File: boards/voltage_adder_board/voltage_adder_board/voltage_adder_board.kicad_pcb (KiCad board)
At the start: 2 copper layers, 95.8 x 94 mm, 30 parts, among them J1 Conn_01x02_Female, J2 Conn_01x04, J3 Conn_01x02_Female, J4 Conn_01x02_Female, J5 Conn_01x03_Female, J6 Conn_01x03_Female, U1 UA741CP, U2 UA741CP, U3 UA741CP

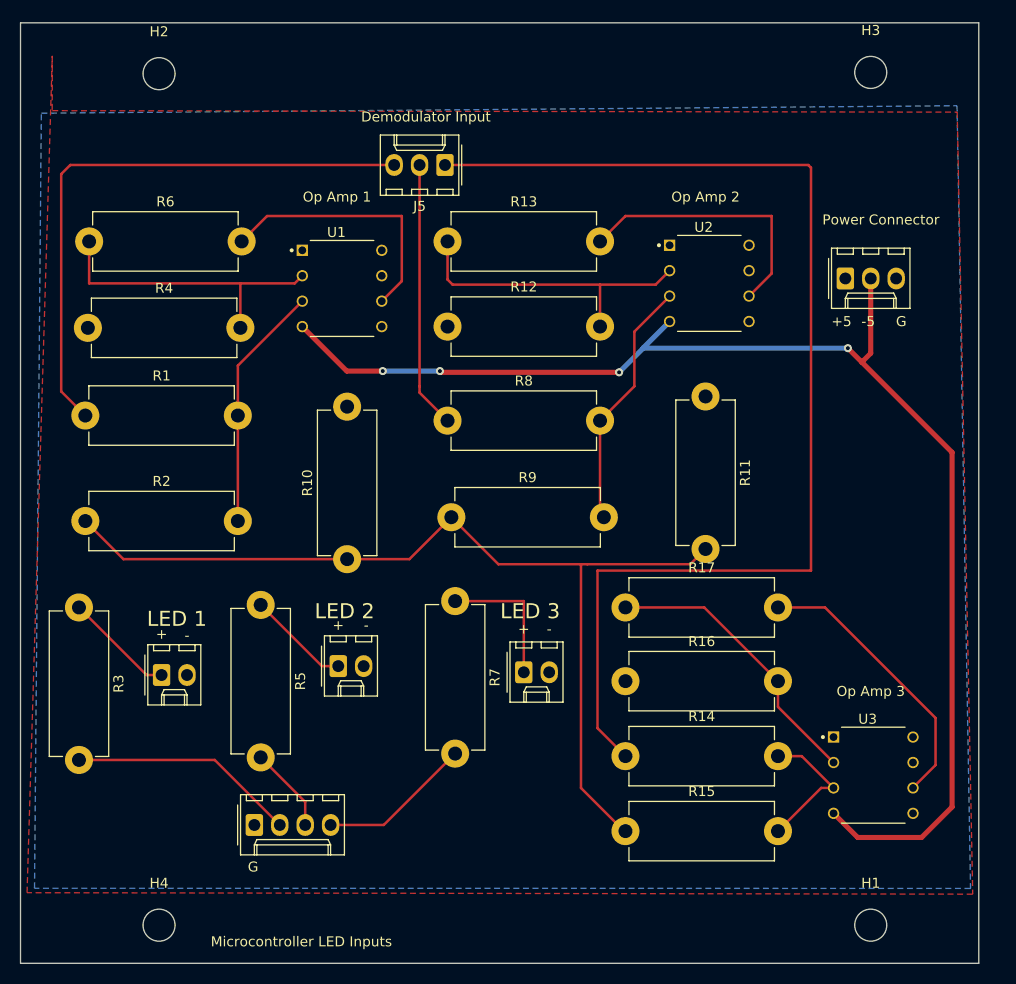
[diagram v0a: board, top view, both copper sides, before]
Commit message: finished voltage adder board
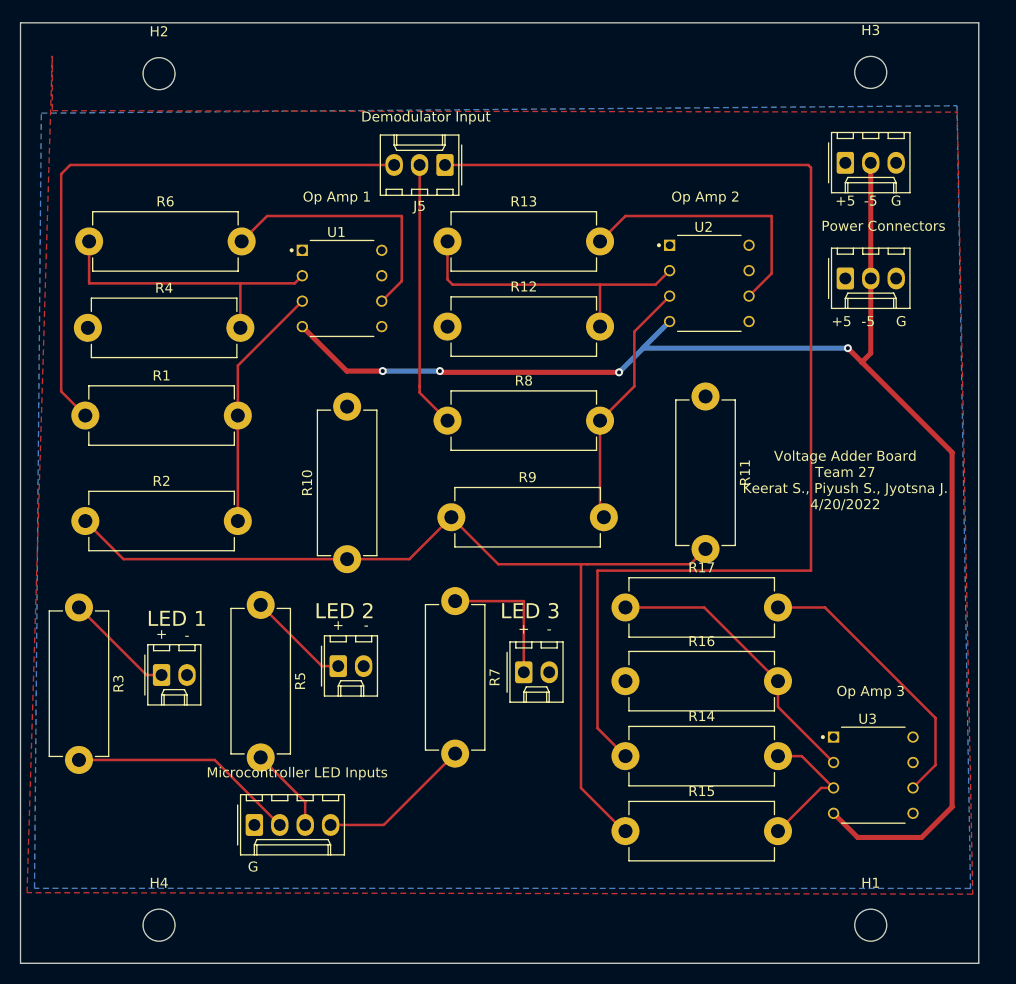
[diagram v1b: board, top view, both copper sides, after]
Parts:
- added J7: Conn_01x03_Female, Connector_Molex:Molex_KK-254_AE-6410-03A_1x03_P2.54mm_Vertical, F.Cu at (144.8, 50.8)
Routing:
- net -5V: track 134.2 -> 145.8 mm
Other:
- board text added: "Power Connectors"
- board text added: "Voltage Adder Board Team 27 Keerat S., Piyush S., Jyotsna J. 4/20/2022"
- board text removed: "Power Connector"
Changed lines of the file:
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@@
   (net 25 "unconnected-(U3-Pad1)")
   (net 26 "unconnected-(U3-Pad5)")
-  (net 27 "Net-(R5-Pad2)")
-  (net 28 "Net-(R7-Pad2)")
+  (net 27 "Net-(J2-Pad3)")
+  (net 28 "Net-(J2-Pad4)")
   (footprint "Resistor_THT:R_Axial_DIN0614_L14.3mm_D5.7mm_P15.24mm_Horizontal" (layer "F.Cu")
     (at 69.088 67.31)
@@
       (net 4 "Net-(J3-Pad1)") (pintype "passive"))
     (pad "2" thru_hole oval (at 15.24 0 270) (size 2.8 2.8) (drill 1.4) (layers *.Cu *.Mask)
-      (net 27 "Net-(R5-Pad2)") (pintype "passive"))
+      (net 27 "Net-(J2-Pad3)") (pintype "passive"))
     (model "${KICAD6_3DMODEL_DIR}/Resistor_THT.3dshapes/R_Axial_DIN0614_L14.3mm_D5.7mm_P15.24mm_Horizontal.wrl"
       (offset (xyz 0 0 0))
@@
     (fp_circle (center 0 0) (end 3.45 0) (layer "F.CrtYd") (width 0.05) (fill none))
     (pad "" np_thru_hole circle (at 0 0) (size 3.2 3.2) (drill 3.2) (layers *.Cu *.Mask))
+  )
+  (footprint "Connector_Molex:Molex_KK-254_AE-6410-03A_1x03_P2.54mm_Vertical" (layer "F.Cu")
+    (at 144.78 50.82)
+    (descr "Molex KK-254 Interconnect System, old/engineering part number: AE-6410-03A example for new part number: 22-27-2031, 3 Pins (http://www.molex.com/pdm_docs/sd/022272021_sd.pdf), generated with kicad-footprint-generator")
+    (tags "connector Molex KK-254 vertical")
+    (property "Sheetfile" "voltage_adder_board.kicad_sch")
+    (property "Sheetname" "")
+    (attr through_hole)
+    (fp_text reference "J7" (at 2.54 -4.12) (layer "F.SilkS") hide
+      (effects (font (size 1 1) (thickness 0.15)))
+    )
+    (fp_text value "Conn_01x03_Female" (at 2.794 4.715) (layer "F.Fab")
+      (effects (font (size 1 1) (thickness 0.15)))
+    )
+    (fp_text user "G" (at 5.08 3.81 unlocked) (layer "F.SilkS")
+      (effects (font (size 1 1) (thickness 0.15)))
+    )
+    (fp_text user "-5" (at 2.54 3.81 unlocked) (layer "F.SilkS")
+      (effects (font (size 1 1) (thickness 0.15)))
+    )
+    (fp_text user "+5" (at 0 3.81 unlocked) (layer "F.SilkS")
+      (effects (font (size 1 1) (thickness 0.15)))
+    )
+    (fp_text user "${REFERENCE}" (at 2.54 -2.22) (layer "F.Fab")
+      (effects (font (size 1 1) (thickness 0.15)))
+    )
+    (fp_line (start 0.8 -2.43) (end 0.8 -3.03) (layer "F.SilkS") (width 0.12))
+    (fp_line (start -1.38 2.99) (end 6.46 2.99) (layer "F.SilkS") (width 0.12))
+    (fp_line (start 4.83 1.46) (end 5.08 1.99) (layer "F.SilkS") (width 0.12))
+    (fp_line (start 0.25 2.99) (end 0.25 1.99) (layer "F.SilkS") (width 0.12))
+    (fp_line (start 4.28 -2.43) (end 5.88 -2.43) (layer "F.SilkS") (width 0.12))
+    (fp_line (start 0.25 1.46) (end 4.83 1.46) (layer "F.SilkS") (width 0.12))
+    (fp_line (start 1.74 -2.43) (end 3.34 -2.43) (layer "F.SilkS") (width 0.12))
+    (fp_line (start -0.8 -3.03) (end -0.8 -2.43) (layer "F.SilkS") (width 0.12))
+    (fp_line (start 0 2.99) (end 0 1.99) (layer "F.SilkS") (width 0.12))
+    (fp_line (start 0 1.99) (end 0.25 1.46) (layer "F.SilkS") (width 0.12))
+    (fp_line (start 4.28 -3.03) (end 4.28 -2.43) (layer "F.SilkS") (width 0.12))
+    (fp_line (start 4.83 2.99) (end 4.83 1.99) (layer "F.SilkS") (width 0.12))
+    (fp_line (start 0 1.99) (end 5.08 1.99) (layer "F.SilkS") (width 0.12))
+    (fp_line (start 5.08 1.99) (end 5.08 2.99) (layer "F.SilkS") (width 0.12))
+    (fp_line (start 3.34 -2.43) (end 3.34 -3.03) (layer "F.SilkS") (width 0.12))
+    (fp_line (start 6.46 2.99) (end 6.46 -3.03) (layer "F.SilkS") (width 0.12))
+    (fp_line (start 5.88 -2.43) (end 5.88 -3.03) (layer "F.SilkS") (width 0.12))
+    (fp_line (start 1.74 -3.03) (end 1.74 -2.43) (layer "F.SilkS") (width 0.12))
+    (fp_line (start 6.46 -3.03) (end -1.38 -3.03) (layer "F.SilkS") (width 0.12))
+    (fp_line (start -1.67 -2) (end -1.67 2) (layer "F.SilkS") (width 0.12))
+    (fp_line (start -0.8 -2.43) (end 0.8 -2.43) (layer "F.SilkS") (width 0.12))
+    (fp_line (start -1.38 -3.03) (end -1.38 2.99) (layer "F.SilkS") (width 0.12))
+    (fp_line (start -1.77 3.38) (end 6.85 3.38) (layer "F.CrtYd") (width 0.05))
+    (fp_line (start -1.77 -3.42) (end -1.77 3.38) (layer "F.CrtYd") (width 0.05))
+    (fp_line (start 6.85 3.38) (end 6.85 -3.42) (layer "F.CrtYd") (width 0.05))
+    (fp_line (start 6.85 -3.42) (end -1.77 -3.42) (layer "F.CrtYd") (width 0.05))
+    (fp_line (start -1.27 -2.92) (end -1.27 2.88) (layer "F.Fab") (width 0.1))
+    (fp_line (start 6.35 -2.92) (end -1.27 -2.92) (layer "F.Fab") (width 0.1))
+    (fp_line (start 6.35 2.88) (end 6.35 -2.92) (layer "F.Fab") (width 0.1))
+    (fp_line (start -0.562893 0) (end -1.27 0.5) (layer "F.Fab") (width 0.1))
+    (fp_line (start -1.27 2.88) (end 6.35 2.88) (layer "F.Fab") (width 0.1))
+    (fp_line (start -1.27 -0.5) (end -0.562893 0) (layer "F.Fab") (width 0.1))
+    (pad "1" thru_hole roundrect (at 0 0) (size 1.74 2.19) (drill 1.19) (layers *.Cu *.Mask) (roundrect_rratio 0.143678)
+      (net 14 "+5V") (pinfunction "Pin_1") (pintype "passive"))
+    (pad "2" thru_hole oval (at 2.54 0) (size 1.74 2.19) (drill 1.19) (layers *.Cu *.Mask)
+      (net 21 "-5V") (pinfunction "Pin_2") (pintype "passive"))
+    (pad "3" thru_hole oval (at 5.08 0) (size 1.74 2.19) (drill 1.19) (layers *.Cu *.Mask)
+      (net 2 "GND") (pinfunction "Pin_3") (pintype "passive"))
+    (model "${KICAD6_3DMODEL_DIR}/Connector_Molex.3dshapes/Molex_KK-254_AE-6410-03A_1x03_P2.54mm_Vertical.wrl"
+      (offset (xyz 0 0 0))
+      (scale (xyz 1 1 1))
+      (rotate (xyz 0 0 0))
+    )
   )
   (footprint "Resistor_THT:R_Axial_DIN0614_L14.3mm_D5.7mm_P15.24mm_Horizontal" (layer "F.Cu")
@@
       (net 3 "Net-(J2-Pad2)") (pinfunction "Pin_2") (pintype "passive"))
     (pad "3" thru_hole oval (at 5.08 0) (size 1.74 2.19) (drill 1.19) (layers *.Cu *.Mask)
-      (net 27 "Net-(R5-Pad2)") (pinfunction "Pin_3") (pintype "passive"))
+      (net 27 "Net-(J2-Pad3)") (pinfunction "Pin_3") (pintype "passive"))
     (pad "4" thru_hole oval (at 7.62 0) (size 1.74 2.19) (drill 1.19) (layers *.Cu *.Mask)
-      (net 28 "Net-(R7-Pad2)") (pinfunction "Pin_4") (pintype "passive"))
+      (net 28 "Net-(J2-Pad4)") (pinfunction "Pin_4") (pintype "passive"))
     (model "${KICAD6_3DMODEL_DIR}/Connector_Molex.3dshapes/Molex_KK-254_AE-6410-04A_1x04_P2.54mm_Vertical.wrl"
       (offset (xyz 0 0 0))
@@
       (net 5 "Net-(J4-Pad1)") (pintype "passive"))
     (pad "2" thru_hole oval (at 15.24 0 270) (size 2.8 2.8) (drill 1.4) (layers *.Cu *.Mask)
-      (net 28 "Net-(R7-Pad2)") (pintype "passive"))
+      (net 28 "Net-(J2-Pad4)") (pintype "passive"))
     (model "${KICAD6_3DMODEL_DIR}/Resistor_THT.3dshapes/R_Axial_DIN0614_L14.3mm_D5.7mm_P15.24mm_Horizontal.wrl"
       (offset (xyz 0 0 0))
@@
     (effects (font (size 1 1) (thickness 0.15)))
   )
+  (gr_text "Voltage Adder Board\nTeam 27\nKeerat S., Piyush S., Jyotsna J.\n4/20/2022" (at 144.78 82.55) (layer "F.SilkS")
+    (effects (font (size 1 1) (thickness 0.15)))
+  )
   (gr_text "Demodulator Input" (at 102.87 46.228) (layer "F.SilkS")
     (effects (font (size 1 1) (thickness 0.15)))
@@
     (effects (font (size 1 1) (thickness 0.15)))
   )
-  (gr_text "Microcontroller LED Inputs" (at 90.424 128.651) (layer "F.SilkS")
+  (gr_text "Microcontroller LED Inputs" (at 90.005 111.76) (layer "F.SilkS")
     (effects (font (size 1 1) (thickness 0.15)))
   )
-  (gr_text "Power Connector" (at 148.336 56.515) (layer "F.SilkS")
+  (gr_text "Power Connectors\n" (at 148.59 57.15) (layer "F.SilkS")
     (effects (font (size 1 1) (thickness 0.15)))
   )
@@
   (segment (start 147.32 69.85) (end 146.431 70.739) (width 0.508) (layer "F.Cu") (net 21))
   (segment (start 147.32 62.377) (end 147.32 69.85) (width 0.508) (layer "F.Cu") (net 21))
+  (segment (start 147.32 50.82) (end 147.32 62.37699) (width 0.508) (layer "F.Cu") (net 21))
   (via (at 145.034 69.342) (size 0.8) (drill 0.4) (layers "F.Cu" "B.Cu") (net 21))
   (via (at 98.552 71.628) (size 0.8) (drill 0.4) (layers "F.Cu" "B.Cu") (net 21))
